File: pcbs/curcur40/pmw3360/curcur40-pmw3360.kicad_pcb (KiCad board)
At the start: 2 copper layers, 23.5 x 33 mm, 20 parts, among them J1 Conn_01x08, U1 PMW3360DM-T2QU, U2 TLV74318PDBVR

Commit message: fail
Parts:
- moved H4 8.19 mm to (158.6, 99.5)
- moved H3 1.50 mm to (154.4, 81.0)
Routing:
- net VDD: track 49.4 -> 53.3 mm
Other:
- board size 23.5 x 33 mm -> 26.5 x 33 mm

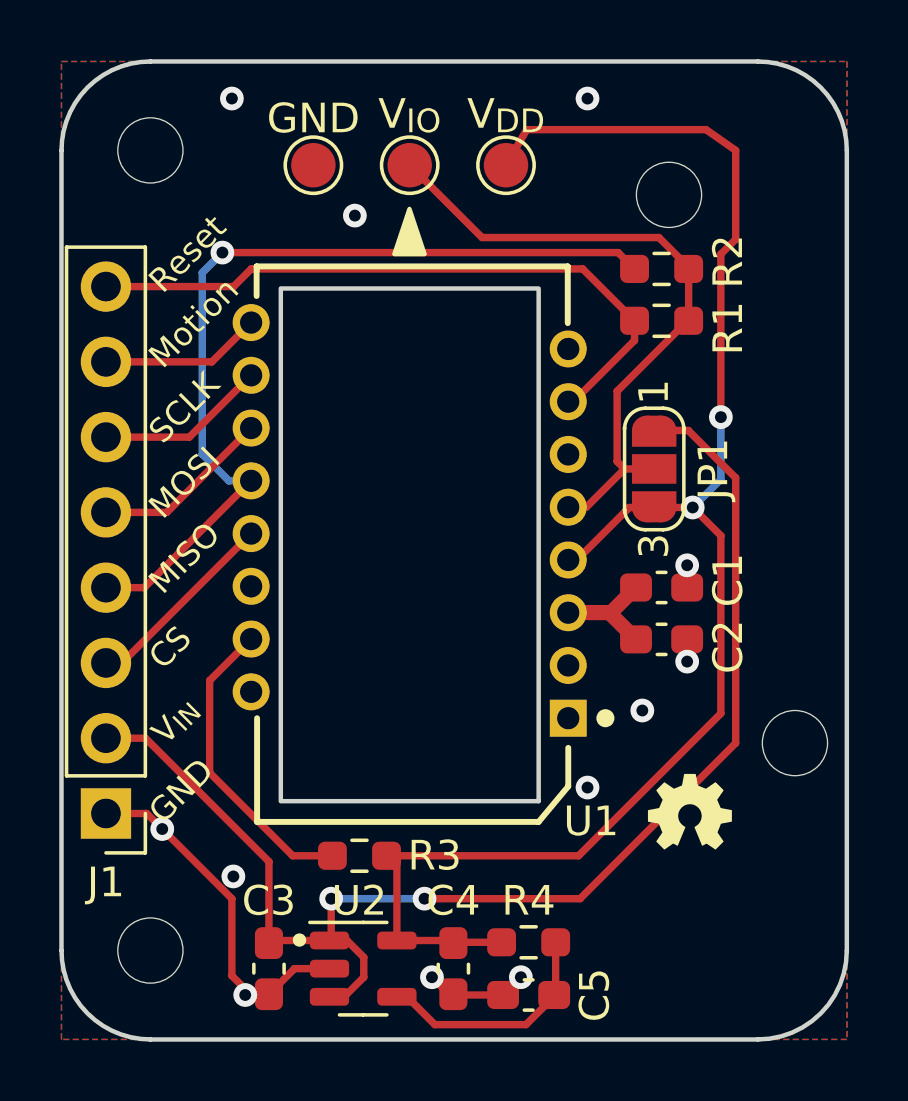
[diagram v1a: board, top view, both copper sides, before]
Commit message: Revert "fail"
This reverts commit f8bb31090bfefcb8a86d31faa946f47e5456d5b7.
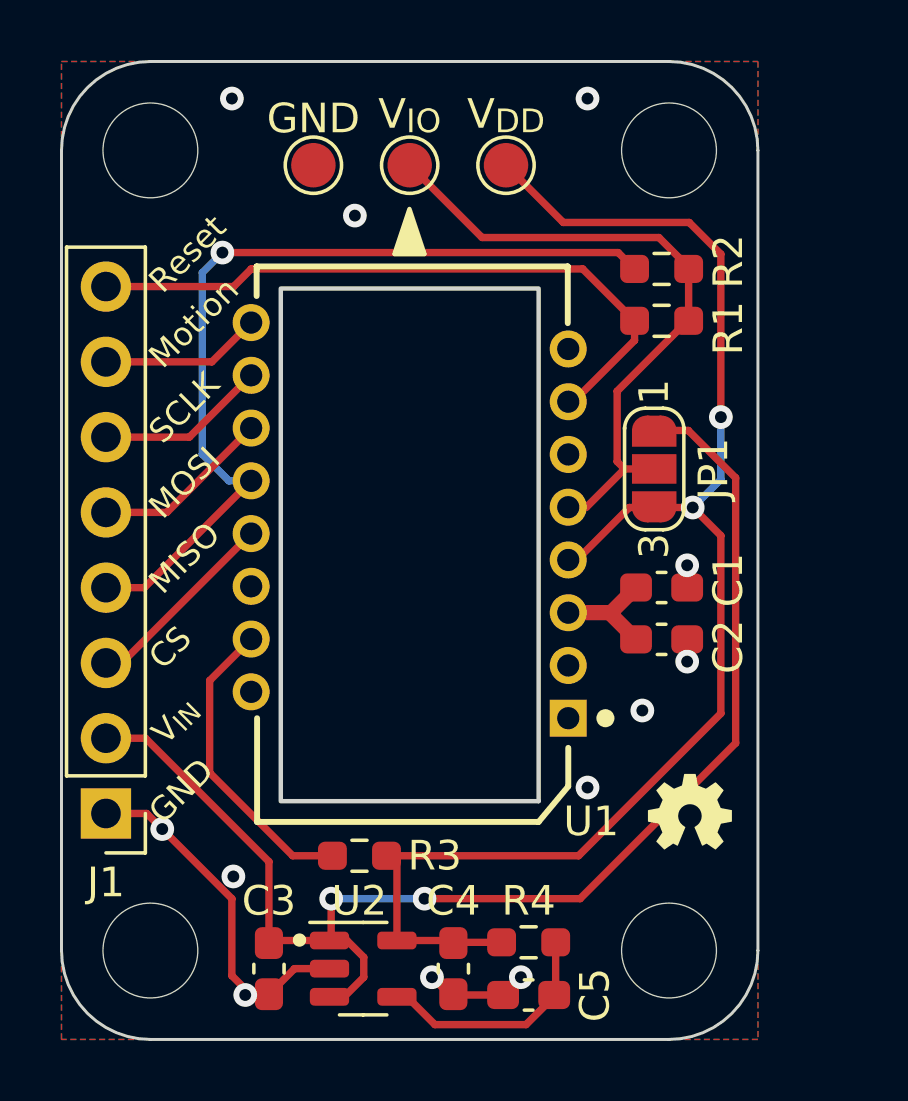
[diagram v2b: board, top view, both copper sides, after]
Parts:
- moved H4 8.19 mm to (154.4, 106.5)
- moved H3 1.50 mm to (154.4, 79.5)
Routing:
- net VDD: track 53.3 -> 49.4 mm
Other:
- board size 26.5 x 33 mm -> 23.5 x 33 mm
